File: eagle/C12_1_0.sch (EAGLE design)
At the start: 11 parts, among them IC1 4040N, X1 Ctrl, X2 Out A, X3 Out B, X4 Out C

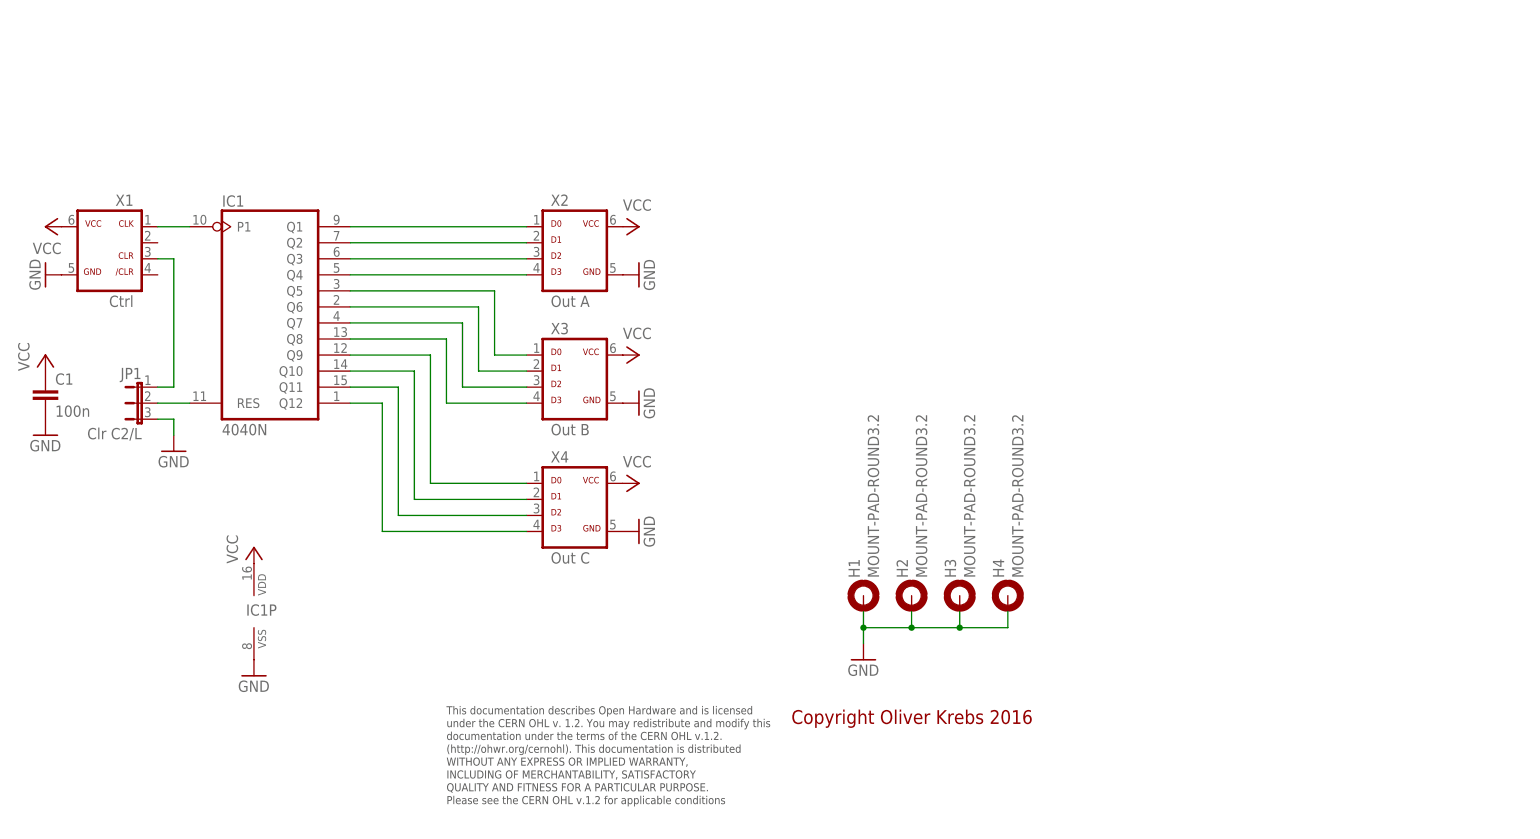
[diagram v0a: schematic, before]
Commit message: Add new tetra-Board and arduino files
Add AMP_1_0, AVC_1_0, D18_1_1, IOP_1_2, MIC_1_0, PIN_1_1, POT_1_0, PWA_1_0, PWR_1_0, RGF 2.0, SOC_2_0, VLT_1_0
Add mex_nano_shield_keyboard, mex_nano_shied_numbers

New arduino projects
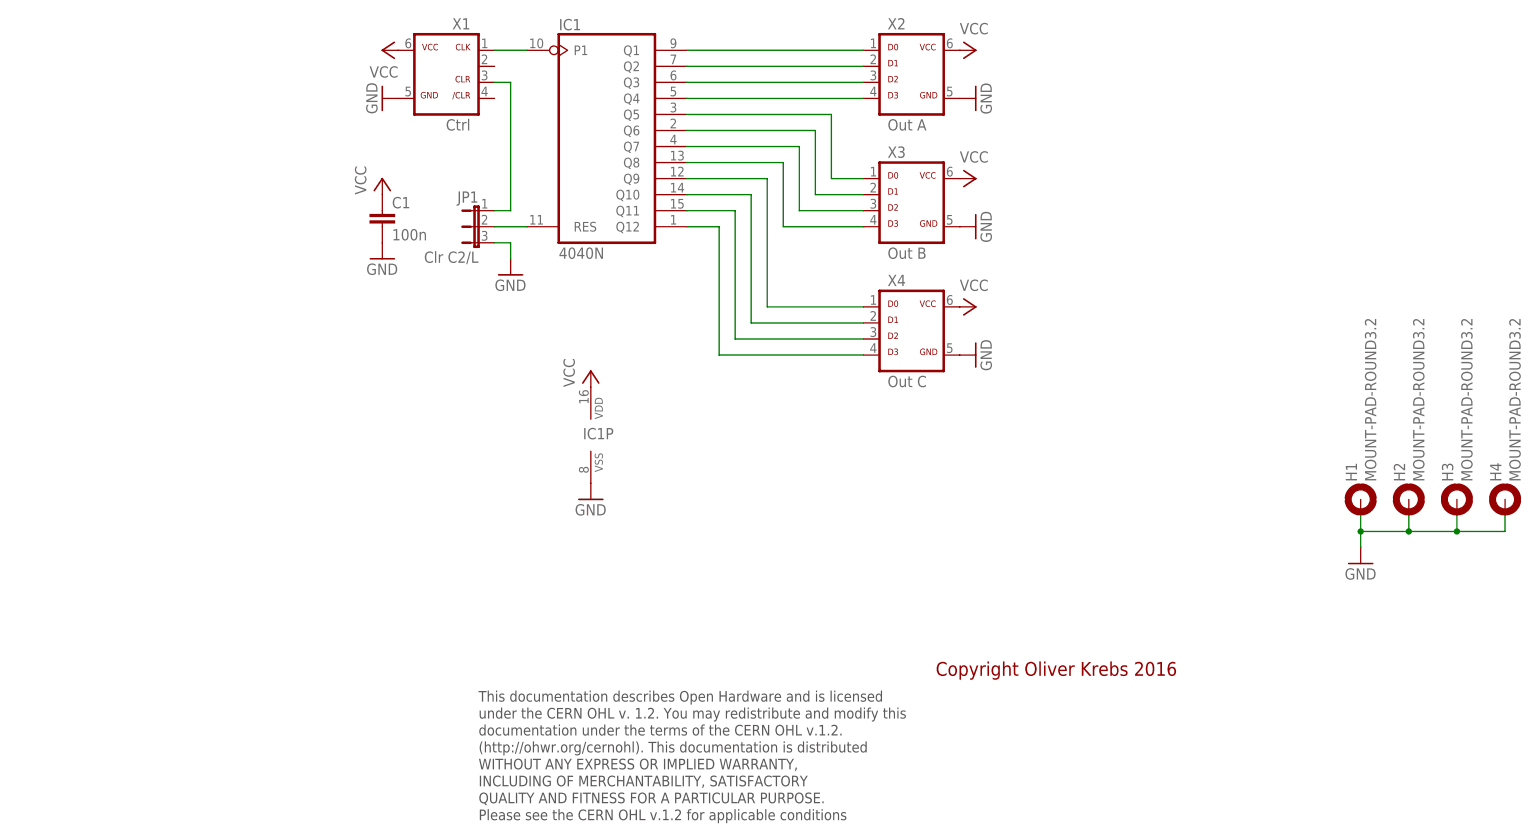
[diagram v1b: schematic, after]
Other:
- moved on the sheet: C1, H1, H2, H3, H4, IC1, IC1P, JP1, X1, X2, X3, X4
